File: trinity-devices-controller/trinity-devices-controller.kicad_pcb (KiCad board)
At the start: 4 copper layers, 90 parts, among them IC1 LM25145RGYR, IC2 MCP2562, J1 xh2pin, J10 xh2pin, J11 Conn_01x03, J12 Conn_01x03, J13 Conn_01x03, J2 xh2pin, J3 Conn_01x01_Pin, J4 Conn_01x01_Pin, J5 Conn_01x04, J6 Conn_01x04, J7 Conn_01x04_Pin, J8 Conn_01x04, J9 xh2pin, Q1 IRFML8244TRPBFTR, Q2 IRFML8244TRPBFTR, Q3 TPH7R506NH,L1Q, Q4 TPH2R306NH1,LQ, Q5 IRFML8244TRPBFTR, Q6 IRFML8244TRPBFTR, SW1 SW_Push, U1 TLP293-4, U3 STM32G431K8Tx, U4 NJM12888F33, U6 NJM7805SDL1, U8 ISO6540FQDBQRQ1

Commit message: 配置、配線完了
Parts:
- added C32: 0.1uf, Capacitor_SMD:C_0603_1608Metric_Pad1.08x0.95mm_HandSolder, F.Cu at (82.0, 45.4)
- added D10: LED, LED_SMD:LED_0603_1608Metric_Pad1.05x0.95mm_HandSolder, F.Cu at (18.1, 69.4)
- added D11: LED, LED_SMD:LED_0603_1608Metric_Pad1.05x0.95mm_HandSolder, F.Cu at (18.1, 71.0)
- added D12: LED, LED_SMD:LED_0603_1608Metric_Pad1.05x0.95mm_HandSolder, F.Cu at (18.1, 72.6)
- added D5: LED, LED_SMD:LED_0603_1608Metric_Pad1.05x0.95mm_HandSolder, F.Cu at (18.1, 60.0)
- added D6: LED, LED_SMD:LED_0603_1608Metric_Pad1.05x0.95mm_HandSolder, F.Cu at (18.1, 61.6)
- added D7: LED, LED_SMD:LED_0603_1608Metric_Pad1.05x0.95mm_HandSolder, F.Cu at (18.1, 63.2)
- added D8: LED, LED_SMD:LED_0603_1608Metric_Pad1.05x0.95mm_HandSolder, F.Cu at (18.1, 64.8)
- added D9: LED, LED_SMD:LED_0603_1608Metric_Pad1.05x0.95mm_HandSolder, F.Cu at (18.1, 67.8)
- added J14: Conn_01x02, Connector_AMASS:AMASS_XT30UPB-M_1x02_P5.0mm_Vertical, F.Cu at (58.0, 18.5)
- added J15: Conn_01x03, Connector_JST:JST_XH_B3B-XH-A_1x03_P2.50mm_Vertical, F.Cu at (30.1, 18.3)
- added R27: 10k, Resistor_SMD:R_0603_1608Metric_Pad0.98x0.95mm_HandSolder, F.Cu at (48.6, 27.2)
- added R28: 10k, Resistor_SMD:R_0603_1608Metric_Pad0.98x0.95mm_HandSolder, F.Cu at (45.2, 27.2)
- added R29: 10k, Resistor_SMD:R_0603_1608Metric_Pad0.98x0.95mm_HandSolder, F.Cu at (41.8, 27.2)
- added R30: 10k, Resistor_SMD:R_0603_1608Metric_Pad0.98x0.95mm_HandSolder, F.Cu at (38.4, 27.2)
- added R31: 10k, Resistor_SMD:R_0603_1608Metric_Pad0.98x0.95mm_HandSolder, F.Cu at (49.0, 49.0)
- added R32: 1k, Resistor_SMD:R_0603_1608Metric_Pad0.98x0.95mm_HandSolder, F.Cu at (21.5, 60.0)
- added R33: 1k, Resistor_SMD:R_0603_1608Metric_Pad0.98x0.95mm_HandSolder, F.Cu at (21.5, 61.6)
- added R34: 1k, Resistor_SMD:R_0603_1608Metric_Pad0.98x0.95mm_HandSolder, F.Cu at (21.5, 63.2)
- added R35: 1k, Resistor_SMD:R_0603_1608Metric_Pad0.98x0.95mm_HandSolder, F.Cu at (21.5, 64.8)
- added R36: 1k, Resistor_SMD:R_0603_1608Metric_Pad0.98x0.95mm_HandSolder, F.Cu at (21.5, 67.8)
- added R37: 1k, Resistor_SMD:R_0603_1608Metric_Pad0.98x0.95mm_HandSolder, F.Cu at (21.5, 69.4)
- added R38: 1k, Resistor_SMD:R_0603_1608Metric_Pad0.98x0.95mm_HandSolder, F.Cu at (21.5, 71.0)
- added R39: 1k, Resistor_SMD:R_0603_1608Metric_Pad0.98x0.95mm_HandSolder, F.Cu at (21.5, 72.6)
- added REF**: MountingHole_3.2mm_M3, MountingHole:MountingHole_3.2mm_M3, F.Cu at (19.0, 19.0)
- added REF**: MountingHole_3.2mm_M3, MountingHole:MountingHole_3.2mm_M3, F.Cu at (19.0, 81.0)
- added REF**: MountingHole_3.2mm_M3, MountingHole:MountingHole_3.2mm_M3, F.Cu at (101.0, 19.0)
- added REF**: MountingHole_3.2mm_M3, MountingHole:MountingHole_3.2mm_M3, F.Cu at (101.0, 81.0)
- J1, J10, J2, J9: footprint Connector_JST:JST_XH_S2B-XH-A_1x02_P2.50mm_Horizontal -> Connector_JST:JST_XH_B2B-XH-A_1x02_P2.50mm_Vertical
- J11, J12, J13: footprint Connector_JST:JST_XH_S3B-XH-A_1x03_P2.50mm_Horizontal -> Connector_JST:JST_XH_B3B-XH-A_1x03_P2.50mm_Vertical
- J5, J6, J8: moved to B.Cu
- moved Q1 73.2 mm to (24.1, 24.7), turned to 180 degrees
- moved Q2 71.2 mm to (24.1, 33.2), turned to 180 degrees
- moved Q5 69.3 mm to (24.1, 41.8), turned to 180 degrees
- moved Q6 67.6 mm to (24.1, 50.4), turned to 180 degrees
- moved D1 63.3 mm to (23.3, 29.2), turned to 90 degrees
- moved D2 62.6 mm to (23.3, 37.8), turned to 90 degrees
- moved D4 62.4 mm to (23.3, 54.9), turned to 90 degrees
- moved D3 62.3 mm to (23.3, 46.3), turned to 90 degrees
- moved Q4 61.7 mm to (93.2, 44.8), turned to 90 degrees
- moved Q3 61.3 mm to (86.6, 45.6), turned to 180 degrees
- moved J5 61.2 mm to (33.4, 75.2), turned to 180 degrees
- moved C14 58.8 mm to (92.4, 67.2)
- moved J10 57.0 mm to (19.2, 51.5), turned to -90 degrees
- moved R22 55.8 mm to (25.3, 53.9), turned to 90 degrees
- moved R19 55.7 mm to (25.3, 45.3), turned to 90 degrees
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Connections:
- C6 pad 1: Net-(C6-Pad1) -> Net-(IC1-COMP)
- C6 pad 2: Net-(IC1-FB) -> Net-(C6-Pad2)
- J11 pad 2: PWM1 -> +12V
- J11 pad 3: +12V -> PWM1
- J12 pad 2: PWM2 -> +12V
- J12 pad 3: +12V -> PWM2
- J13 pad 2: PWM3 -> +12V
- J13 pad 3: +12V -> PWM3
- R14 pad 1: Net-(IC1-COMP) -> Net-(C6-Pad2)
- R14 pad 2: Net-(C6-Pad1) -> Net-(IC1-FB)
- R24 pad 1: TIM2_CH3 -> TIM2_CH2
- R25 pad 1: TIM2_CH2 -> TIM2_CH3
- R26 pad 1: TIM2_CH1 -> TIM2_CH4
- U1 pad 1: Net-(R1-Pad2) -> Net-(R21-Pad2)
- U1 pad 11: Net-(R19-Pad1) -> Net-(R3-Pad1)
- U1 pad 13: Net-(R4-Pad1) -> Net-(R19-Pad1)
- U1 pad 15: Net-(R3-Pad1) -> Net-(R22-Pad1)
- U1 pad 3: Net-(R2-Pad2) -> Net-(R18-Pad2)
- U1 pad 5: Net-(R18-Pad2) -> Net-(R1-Pad2)
- U1 pad 7: Net-(R21-Pad2) -> Net-(R2-Pad2)
- U1 pad 9: Net-(R22-Pad1) -> Net-(R4-Pad1)
- U3 pad 10: IN2 -> IN1
- U3 pad 8: unconnected-(U3-PA3-Pad8) -> TIM2_CH4
- U3 pad 9: IN1 -> IN2
- U8 pad 11: unconnected-(U8-OUTD-Pad11) -> PWM1
- U8 pad 12: PWM3 -> PWM2
- U8 pad 13: PWM2 -> PWM3
- U8 pad 14: PWM1 -> PWM4
- U8 pad 3: TIM2_CH1 -> TIM2_CH4
- U8 pad 4: TIM2_CH2 -> TIM2_CH3
- U8 pad 5: TIM2_CH3 -> TIM2_CH2
- U8 pad 6: unconnected-(U8-IND-Pad6) -> TIM2_CH1
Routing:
- net VCC: track 0.00 -> 106.7 mm, vias 0 -> 2
- net +3.3V: track 0.00 -> 104.2 mm, vias 0 -> 5
- net +12V: track 0.00 -> 103.5 mm
- net TIM2_CH2: track 0.00 -> 54.5 mm, vias 0 -> 2
- net TIM2_CH3: track 0.00 -> 53.4 mm, vias 0 -> 2
- net TIM2_CH4: track 0.00 -> 52.1 mm, vias 0 -> 2
- net TIM2_CH1: track 0.00 -> 50.0 mm, vias 0 -> 2
- net +5V: track 0.00 -> 40.7 mm, vias 0 -> 1
- net IN2: track 0.00 -> 35.4 mm, vias 0 -> 2
- net IN1: track 0.00 -> 31.5 mm, vias 0 -> 2
- net CANH: track 0.00 -> 31.1 mm
- net IN3: track 0.00 -> 31.0 mm, vias 0 -> 2
- net IN4: track 0.00 -> 28.9 mm, vias 0 -> 2
- net CANL: track 0.00 -> 26.9 mm
- net SWCLK: track 0.00 -> 26.0 mm, vias 0 -> 1
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- added copper zone on B.Cu, net +12V
- added copper zone on F.Cu, net +12V
- added copper zone on In1.Cu, net +12V
- added copper zone on In2.Cu, net +12V
- added copper zone on B.Cu, net GND
- added copper zone on F.Cu, net GND
- added copper zone on In1.Cu, net GND
- added copper zone on In2.Cu, net GND
- added copper zone on B.Cu, net GNDD
- added copper zone on F.Cu, net GNDD
- added copper zone on In1.Cu, net GNDD
- added copper zone on In2.Cu, net GNDD
- added copper zone on F.Cu, net Net-(IC1-SW)
- added copper zone on F.Cu, net VCC
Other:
- board outline added: 90 x 70 mm
- board text added: "1 2 3 4"
- board text added: "4 3 2 1"
- board text added: "Servo"
- board text added: "Solenoid"

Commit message: ビア以外完成
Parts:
- added D13: LED, LED_SMD:LED_0603_1608Metric_Pad1.05x0.95mm_HandSolder, F.Cu at (61.6, 81.6)
- added D14: LED, LED_SMD:LED_0603_1608Metric_Pad1.05x0.95mm_HandSolder, F.Cu at (60.0, 81.6)
- added D15: LED, LED_SMD:LED_0603_1608Metric_Pad1.05x0.95mm_HandSolder, F.Cu at (63.2, 81.6)
- added D16: LED, LED_SMD:LED_0603_1608Metric_Pad1.05x0.95mm_HandSolder, F.Cu at (23.8, 81.5)
- added D17: LED, LED_SMD:LED_0603_1608Metric_Pad1.05x0.95mm_HandSolder, F.Cu at (25.4, 81.5)
- added R40: 1k, Resistor_SMD:R_0603_1608Metric_Pad0.98x0.95mm_HandSolder, F.Cu at (61.6, 78.2)
- added R41: 1k, Resistor_SMD:R_0603_1608Metric_Pad0.98x0.95mm_HandSolder, F.Cu at (60.0, 78.2)
- added R42: 1k, Resistor_SMD:R_0603_1608Metric_Pad0.98x0.95mm_HandSolder, F.Cu at (63.2, 78.2)
- added R43: 1k, Resistor_SMD:R_0603_1608Metric_Pad0.98x0.95mm_HandSolder, F.Cu at (23.8, 78.1)
- added R44: 1k, Resistor_SMD:R_0603_1608Metric_Pad0.98x0.95mm_HandSolder, F.Cu at (25.4, 78.1)
- moved J4 1.20 mm to (70.0, 87.7)
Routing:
- net +5P: track 13.3 -> 63.6 mm
- net +12V: track 103.5 -> 150.1 mm
- net VCC: track 106.7 -> 121.1 mm, vias 2 -> 3
- net +3.3V: track 104.2 -> 116.9 mm
- net +5V: track 40.7 -> 44.0 mm
- net Net-(D17-A): track 0.00 -> 1.61 mm
- net Net-(D16-A): track 0.00 -> 1.61 mm
- net Net-(D15-A): track 0.00 -> 1.61 mm
- net Net-(D14-A): track 0.00 -> 1.61 mm
- net Net-(D13-A): track 0.00 -> 1.61 mm
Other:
- board text added: "12"
- board text added: "3.3 5"
- board text added: "5"
- board text added: "VCC"

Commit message: 完成、ガーバー作成完了
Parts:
- added D18: LED, LED_SMD:LED_0603_1608Metric_Pad1.05x0.95mm_HandSolder, F.Cu at (44.2, 81.5)
- added D19: LED, LED_SMD:LED_0603_1608Metric_Pad1.05x0.95mm_HandSolder, F.Cu at (45.8, 81.5)
- added D20: LED, LED_SMD:LED_0603_1608Metric_Pad1.05x0.95mm_HandSolder, F.Cu at (47.4, 81.5)
- added D21: LED, LED_SMD:LED_0603_1608Metric_Pad1.05x0.95mm_HandSolder, F.Cu at (49.0, 81.5)
- added G***: LOGO, LOGO, F.Cu at (61.3, 54.8)
- added R45: 1k, Resistor_SMD:R_0603_1608Metric_Pad0.98x0.95mm_HandSolder, F.Cu at (44.2, 78.1)
- added R46: 1k, Resistor_SMD:R_0603_1608Metric_Pad0.98x0.95mm_HandSolder, F.Cu at (45.8, 78.1)
- added R47: 1k, Resistor_SMD:R_0603_1608Metric_Pad0.98x0.95mm_HandSolder, F.Cu at (47.4, 78.1)
- added R48: 1k, Resistor_SMD:R_0603_1608Metric_Pad0.98x0.95mm_HandSolder, F.Cu at (49.0, 78.1)
- moved C26 2.25 mm to (30.8, 81.7)
- moved C27 2.25 mm to (37.1, 81.8)
- moved U4 2.25 mm to (34.0, 81.8)
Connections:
- U3 pad 18: unconnected-(U3-PA8-Pad18) -> LED4
- U3 pad 19: unconnected-(U3-PA9-Pad19) -> LED3
- U3 pad 20: unconnected-(U3-PA10-Pad20) -> LED2
- U3 pad 28: unconnected-(U3-PB5-Pad28) -> LED1
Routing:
- net LED4: track 0.00 -> 22.7 mm, vias 0 -> 2
- net LED3: track 0.00 -> 21.7 mm, vias 0 -> 2
- net LED2: track 0.00 -> 19.7 mm, vias 0 -> 2
- net LED1: track 0.00 -> 11.9 mm, vias 0 -> 2
- net +3.3V: track 116.9 -> 118.7 mm
- net Net-(D21-A): track 0.00 -> 1.61 mm
- net Net-(D20-A): track 0.00 -> 1.61 mm
- net Net-(D19-A): track 0.00 -> 1.61 mm
- net Net-(D18-A): track 0.00 -> 1.61 mm
- net GNDD: vias 11 -> 66
- net GND: vias 23 -> 359
- net +12V: vias 0 -> 82
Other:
- board text added: "3.3"
- board text added: "CAN"
- board text added: "CLK"
- board text added: "DIO"
- board text added: "G"
- board text added: "G T 3.3 R"
- board text added: "GND"
- board text added: "H 5 L G"
- board text added: "LED"
- board text added: "UART"
- board text added: "trinity-devices-controller version 1.0 create by ikeda"

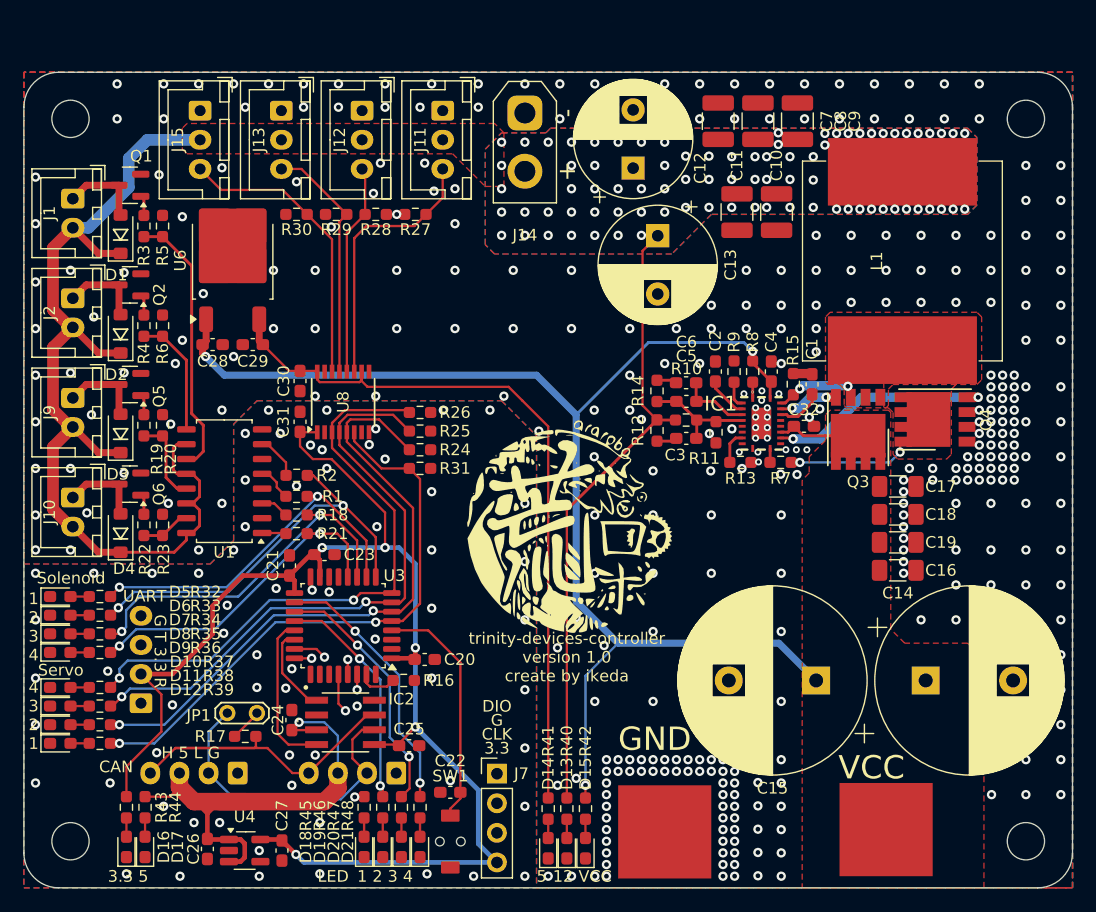
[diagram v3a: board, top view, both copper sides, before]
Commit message: VCCのトラブル修正、仕様の一部を変更
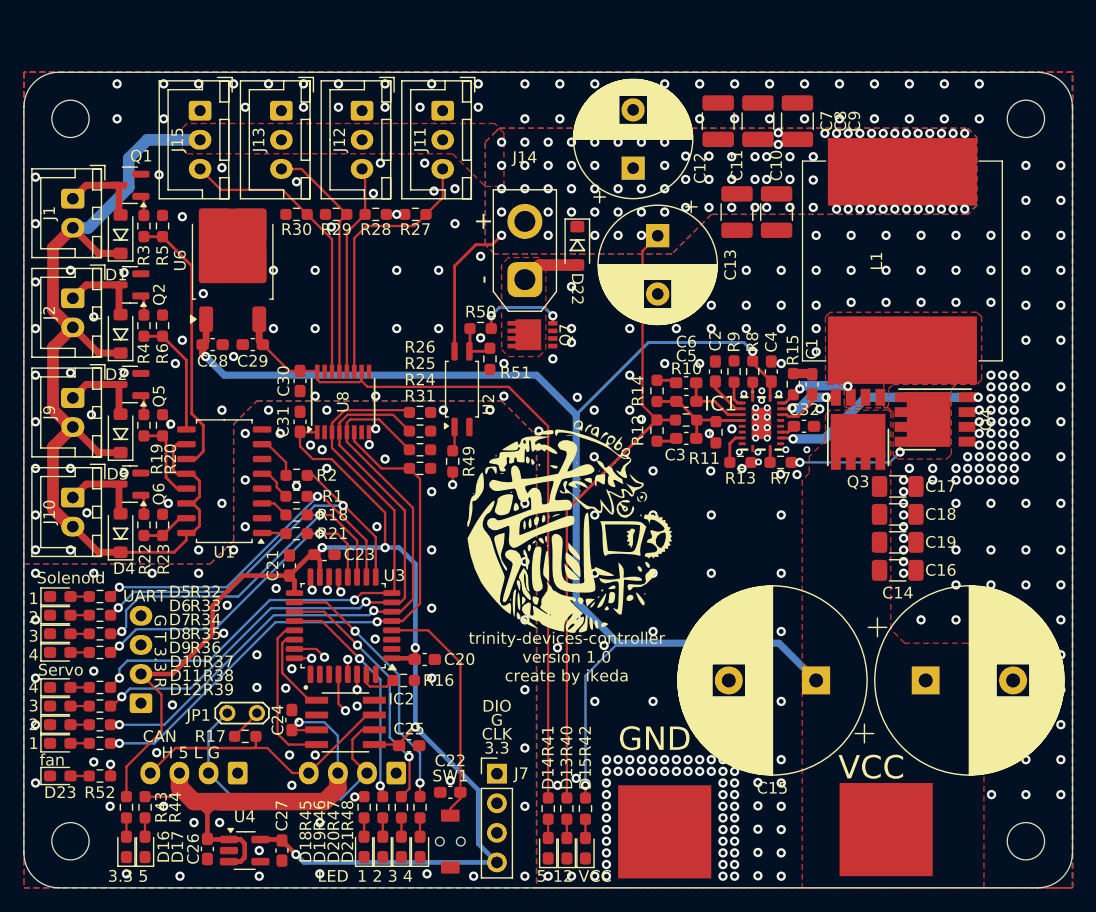
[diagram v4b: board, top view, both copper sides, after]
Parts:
- added D22: SS2040FL, 0Ikedalibrary:SOD-123FL, F.Cu at (62.5, 29.6)
- added D23: LED, LED_SMD:LED_0603_1608Metric_Pad1.05x0.95mm_HandSolder, F.Cu at (18.1, 75.4)
- added Q7: TPN1R603PL, 0Ikedalibrary:TSON Advance, F.Cu at (58.3, 37.5)
- added R49: 10k, Resistor_SMD:R_0603_1608Metric_Pad0.98x0.95mm_HandSolder, F.Cu at (51.8, 48.4)
- added R50: 100, Resistor_SMD:R_0603_1608Metric_Pad0.98x0.95mm_HandSolder, F.Cu at (54.2, 37.0)
- added R51: 10k, Resistor_SMD:R_0603_1608Metric_Pad0.98x0.95mm_HandSolder, F.Cu at (55.0, 39.6)
- added R52: 1k, Resistor_SMD:R_0603_1608Metric_Pad0.98x0.95mm_HandSolder, F.Cu at (21.5, 75.4)
- added U2: TLP293, Package_SO:SOIC-4_4.55x2.6mm_P1.27mm, F.Cu at (52.6, 42.2)
- moved J14 14.3 mm to (58.0, 32.8), turned to 90 degrees
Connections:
- C32 pad 1: VCC -> Net-(IC1-VCC)
- IC1 pad 14: VCC -> Net-(IC1-VCC)
- J14 pad 1: GND -> Net-(D22-A)
- U3 pad 13: unconnected-(U3-PB0-Pad13) -> fan
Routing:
- net fan: track 0.00 -> 56.5 mm, vias 0 -> 3
- net +12V: track 150.1 -> 162.6 mm
- net Net-(Q7-G): track 0.00 -> 7.62 mm, vias 0 -> 2
- net VCC: track 121.1 -> 113.9 mm
- net Net-(D22-A): track 0.00 -> 5.02 mm
- net Net-(R50-Pad1): track 0.00 -> 3.85 mm
- net Net-(R49-Pad2): track 0.00 -> 2.11 mm
- net Net-(D23-A): track 0.00 -> 1.61 mm
- net Net-(IC1-VCC): track 0.00 -> 1.34 mm
- net GND: track 0.94 -> 0.00 mm, vias 359 -> 362
- net GNDD: vias 66 -> 67
- added copper zone on F.Cu, net Net-(D22-A)
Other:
- board text added: "fan"

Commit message: 電磁弁の個数変更
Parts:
- added D24: LED, LED_SMD:LED_0603_1608Metric_Pad1.05x0.95mm_HandSolder, F.Cu at (30.6, 61.6)
- added D25: LED, LED_SMD:LED_0603_1608Metric_Pad1.05x0.95mm_HandSolder, F.Cu at (30.6, 63.2)
- added D26: LED, LED_SMD:LED_0603_1608Metric_Pad1.05x0.95mm_HandSolder, F.Cu at (30.6, 64.8)
- added D27: SS2040FL, 0Ikedalibrary:SOD-123FL, F.Cu at (44.6, 29.0)
- added D28: SS2040FL, 0Ikedalibrary:SOD-123FL, F.Cu at (44.6, 34.0)
- added D29: SS2040FL, 0Ikedalibrary:SOD-123FL, F.Cu at (29.2, 41.6)
- added D30: SS2040FL, 0Ikedalibrary:SOD-123FL, F.Cu at (44.6, 38.6)
- added J16: xh2pin, Connector_JST:JST_XH_B2B-XH-A_1x02_P2.50mm_Vertical, F.Cu at (29.2, 29.4)
- added J17: xh2pin, Connector_JST:JST_XH_B2B-XH-A_1x02_P2.50mm_Vertical, F.Cu at (37.8, 29.4)
- added J18: xh2pin, Connector_JST:JST_XH_B2B-XH-A_1x02_P2.50mm_Vertical, F.Cu at (29.2, 36.4)
- added J19: xh2pin, Connector_JST:JST_XH_B2B-XH-A_1x02_P2.50mm_Vertical, F.Cu at (37.8, 36.4)
- added Q10: IRFML8244TRPBFTR, Package_TO_SOT_SMD:SOT-23, F.Cu at (34.9, 42.4)
- added Q11: IRFML8244TRPBFTR, Package_TO_SOT_SMD:SOT-23, F.Cu at (51.2, 38.8)
- added Q8: IRFML8244TRPBFTR, Package_TO_SOT_SMD:SOT-23, F.Cu at (51.2, 31.6)
- added Q9: IRFML8244TRPBFTR, Package_TO_SOT_SMD:SOT-23, F.Cu at (51.2, 35.2)
- added R53: 1k, Resistor_SMD:R_0603_1608Metric_Pad0.98x0.95mm_HandSolder, F.Cu at (34.0, 61.6)
- added R54: 1k, Resistor_SMD:R_0603_1608Metric_Pad0.98x0.95mm_HandSolder, F.Cu at (34.0, 63.2)
- added R55: 1k, Resistor_SMD:R_0603_1608Metric_Pad0.98x0.95mm_HandSolder, F.Cu at (34.0, 64.8)
- added R56: 10k, Resistor_SMD:R_0603_1608Metric_Pad0.98x0.95mm_HandSolder, F.Cu at (46.0, 51.3)
- added R57: 10k, Resistor_SMD:R_0603_1608Metric_Pad0.98x0.95mm_HandSolder, F.Cu at (42.6, 51.3)
- added R58: 10k, Resistor_SMD:R_0603_1608Metric_Pad0.98x0.95mm_HandSolder, F.Cu at (39.2, 51.3)
- added R59: 10k, Resistor_SMD:R_0603_1608Metric_Pad0.98x0.95mm_HandSolder, F.Cu at (46.8, 53.0)
- added R60: 100, Resistor_SMD:R_0603_1608Metric_Pad0.98x0.95mm_HandSolder, F.Cu at (48.4, 31.6)
- added R61: 100, Resistor_SMD:R_0603_1608Metric_Pad0.98x0.95mm_HandSolder, F.Cu at (48.4, 35.2)
- added R62: 100, Resistor_SMD:R_0603_1608Metric_Pad0.98x0.95mm_HandSolder, F.Cu at (32.1, 42.3)
- added R63: 100, Resistor_SMD:R_0603_1608Metric_Pad0.98x0.95mm_HandSolder, F.Cu at (48.4, 38.8)
- added R64: 10k, Resistor_SMD:R_0603_1608Metric_Pad0.98x0.95mm_HandSolder, F.Cu at (46.8, 31.6)
- added R65: 10k, Resistor_SMD:R_0603_1608Metric_Pad0.98x0.95mm_HandSolder, F.Cu at (46.8, 35.2)
- added R66: 10k, Resistor_SMD:R_0603_1608Metric_Pad0.98x0.95mm_HandSolder, F.Cu at (29.6, 43.8)
- added R67: 10k, Resistor_SMD:R_0603_1608Metric_Pad0.98x0.95mm_HandSolder, F.Cu at (46.8, 38.8)
- added U5: TLP293-4, Package_SO:SOIC-16_4.55x10.3mm_P1.27mm, F.Cu at (42.8, 46.2)
- moved U6 39.8 mm to (63.9, 56.1), turned to -90 degrees
- moved C28 36.0 mm to (65.6, 48.9), turned to 180 degrees
- moved C29 29.5 mm to (62.2, 48.9), turned to 0 degrees
- moved D21 28.3 mm to (30.6, 60.0), turned to 0 degrees
- moved R48 23.5 mm to (34.0, 60.0), turned to 180 degrees
- moved G*** 15.5 mm to (76.6, 52.6)
- moved R30 10.7 mm to (49.0, 28.7), turned to 180 degrees
- moved C31 10.6 mm to (49.2, 46.3)
- moved C30 10.6 mm to (49.2, 42.6)
- moved U8 10.6 mm to (52.9, 44.6)
- moved R1 9.39 mm to (46.8, 55.6), turned to 90 degrees
- moved R2 9.06 mm to (45.2, 55.6), turned to 90 degrees
- moved R51 8.64 mm to (61.9, 44.8), turned to 0 degrees
- moved R50 7.69 mm to (60.7, 41.1)
- moved R28 7.35 mm to (52.4, 28.7), turned to 0 degrees
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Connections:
- net LED4 renamed IN5
- U1 pad 11: Net-(R3-Pad1) -> Net-(R4-Pad1)
- U1 pad 5: Net-(R1-Pad2) -> Net-(R2-Pad2)
- U1 pad 7: Net-(R2-Pad2) -> Net-(R1-Pad2)
- U1 pad 9: Net-(R4-Pad1) -> Net-(R3-Pad1)
- U3 pad 10: IN1 -> IN2
- U3 pad 19: LED3 -> IN6
- U3 pad 20: LED2 -> IN7
- U3 pad 25: unconnected-(U3-PA15-Pad25) -> LED2
- U3 pad 26: unconnected-(U3-PB3-Pad26) -> LED3
- U3 pad 27: unconnected-(U3-PB4-Pad27) -> LED1
- U3 pad 28: LED1 -> IN8
- U3 pad 9: IN2 -> IN1
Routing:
- net +12V: track 162.6 -> 227.2 mm
- net IN8: track 0.00 -> 30.5 mm, vias 0 -> 3
- net VCC: track 113.9 -> 84.8 mm
- net OUT5: track 0.00 -> 27.9 mm, vias 0 -> 2
- net IN7: track 0.00 -> 21.7 mm, vias 0 -> 2
- net IN6: track 0.00 -> 20.2 mm, vias 0 -> 2
- net Net-(R60-Pad1): track 0.00 -> 17.6 mm, vias 0 -> 2
- net OUT6: track 0.00 -> 17.6 mm, vias 0 -> 2
- net OUT8: track 0.00 -> 17.5 mm, vias 0 -> 2
- net OUT7: track 0.00 -> 14.9 mm, vias 0 -> 2
- net Net-(R1-Pad2): track 3.08 -> 17.0 mm
- net PWM4: track 25.2 -> 38.6 mm
- net Net-(R61-Pad1): track 0.00 -> 13.1 mm, vias 0 -> 2
- net PWM3: track 21.0 -> 32.4 mm
- net Net-(R62-Pad1): track 0.00 -> 10.5 mm
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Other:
- board text added: "1"
- board text added: "1 2 3"
- board text added: "2"
- board text added: "3"
- board text added: "4"
- board text added: "5 6 7 8"
- board text added: "6"
- board text added: "7"
- board text added: "8"
- board text added: "Servo 4321"

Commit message: シルク、ビアの修正
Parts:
- moved R51 2.42 mm to (60.7, 42.7)
- turned R17 to 0 degrees
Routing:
- net Net-(R50-Pad1): track 5.98 -> 3.38 mm
- net IN7: track 21.7 -> 19.3 mm
- net +12V: track 227.2 -> 225.4 mm, vias 82 -> 64
- net CANH: track 31.1 -> 29.3 mm
- net Net-(Q2-G): track 2.90 -> 1.75 mm
- net LED1: track 12.6 -> 13.8 mm
- net Net-(JP1-A): track 2.79 -> 2.04 mm
- net GNDD: vias 48 -> 57
- net GND: vias 343 -> 352
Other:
- board text added: "trinity-devices-controller version 1.1 create by ikeda"
- board text removed: "trinity-devices-controller version 1.0 create by ikeda"
